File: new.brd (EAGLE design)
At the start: 108.9 x 88.9 mm, 44 parts, among them K1 351, K2 351, K3 351, K4 351, K5 351, K6 351

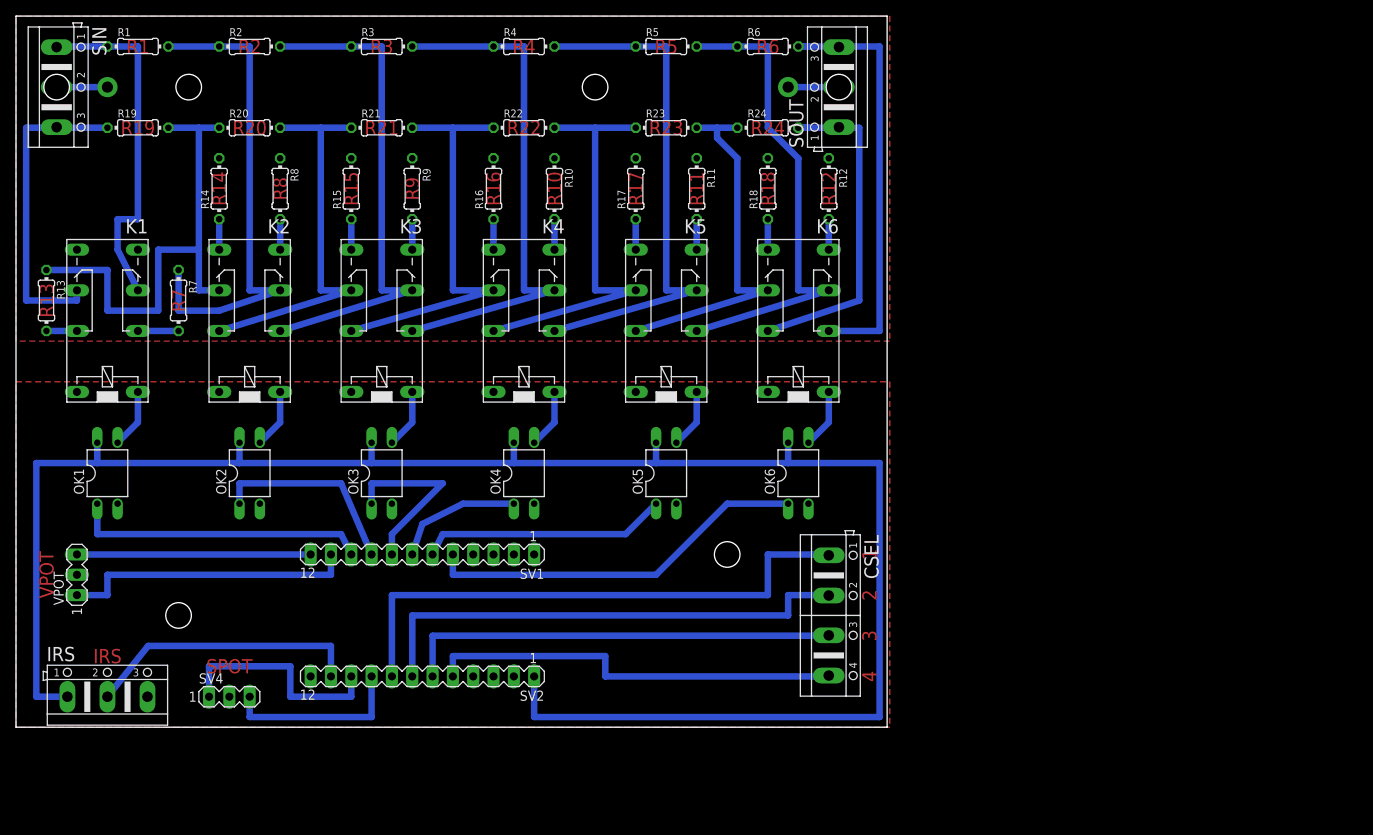
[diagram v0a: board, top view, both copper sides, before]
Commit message: Added gainclone to scheme
Need to add control for mute relay
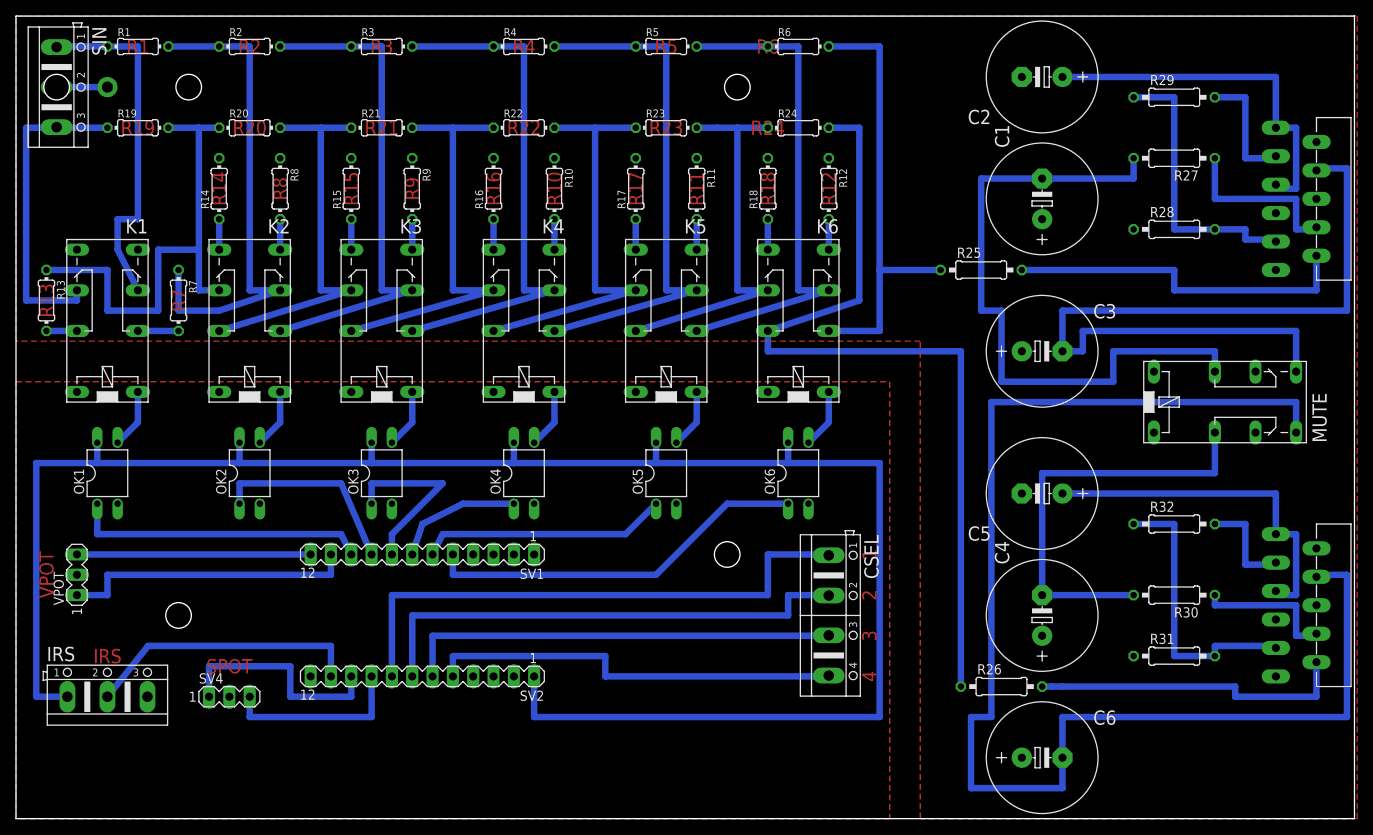
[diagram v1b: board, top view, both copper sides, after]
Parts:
- removed SOUT: (no value), con-ptr500:AK500/3
- added C1, C2, C3, C4, C5, C6: (no value), rcl:E5-13
- added MUTE: 351, relay:351
- added R25, R26, R27, R28, R29, R30, R31, R32: (no value), rcl:0207/10
- added U$1, U$2: (no value), LM3886:TO220-11
- moved R24 3.81 mm to (96.5, 71.1)
- moved R6 3.81 mm to (96.5, 81.3)
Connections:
- new net N$47: R25.2, U$1.10
- new net N$48: C6.-, MUTE.S1, U$2.4
- new net N$51: R28.2, R29.1, U$1.9
- new net N$52: R29.2, U$1.3
- new net N$53: C2.+, U$1.1, U$1.5
- new net N$55: R27.1, U$1.8
- new net N$56: C1.-, MUTE.P2, R27.2
- new net N$57: C3.-, MUTE.S2, U$1.4
- new net N$58: R26.2, U$2.10
- new net N$60: R32.2, U$2.3
- new net N$61: C5.+, U$2.1, U$2.5
- new net N$62: R31.2, R32.1, U$2.9
- new net N$64: R30.1, U$2.8
- new net N$65: C4.-, MUTE.P1, R30.2
- net GNDA: now also C1.+, C2.-, C3.+, C4.+, C5.-, C6.+, R28.1, R31.1, U$1.7, U$2.7; no longer SOUT.2
- net N$32: now also R26.1; no longer SOUT.1
- net N$6: now also R25.1; no longer SOUT.3
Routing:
- net N$48: track 0.00 -> 170.2 mm
- net N$57: track 0.00 -> 99.1 mm
- net N$56: track 0.00 -> 82.6 mm
- net N$32: track 42.5 -> 106.0 mm
- net N$65: track 0.00 -> 53.3 mm
- net N$53: track 0.00 -> 45.7 mm
- net N$61: track 0.00 -> 44.5 mm
- net N$47: track 0.00 -> 43.2 mm
- net N$58: track 0.00 -> 39.4 mm
- net N$51: track 0.00 -> 35.6 mm
- net N$62: track 0.00 -> 35.6 mm
- net N$55: track 0.00 -> 21.6 mm
- net N$64: track 0.00 -> 17.8 mm
- net N$52: track 0.00 -> 15.2 mm
- net N$60: track 0.00 -> 12.7 mm
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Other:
- board size 108.9 x 88.9 mm -> 167.3 x 100.3 mm
